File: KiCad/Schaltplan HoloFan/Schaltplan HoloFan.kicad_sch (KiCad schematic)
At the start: 23 parts, among them Q1 2N3904, Q2 2N3904, U1 NUCLEO-L432KC

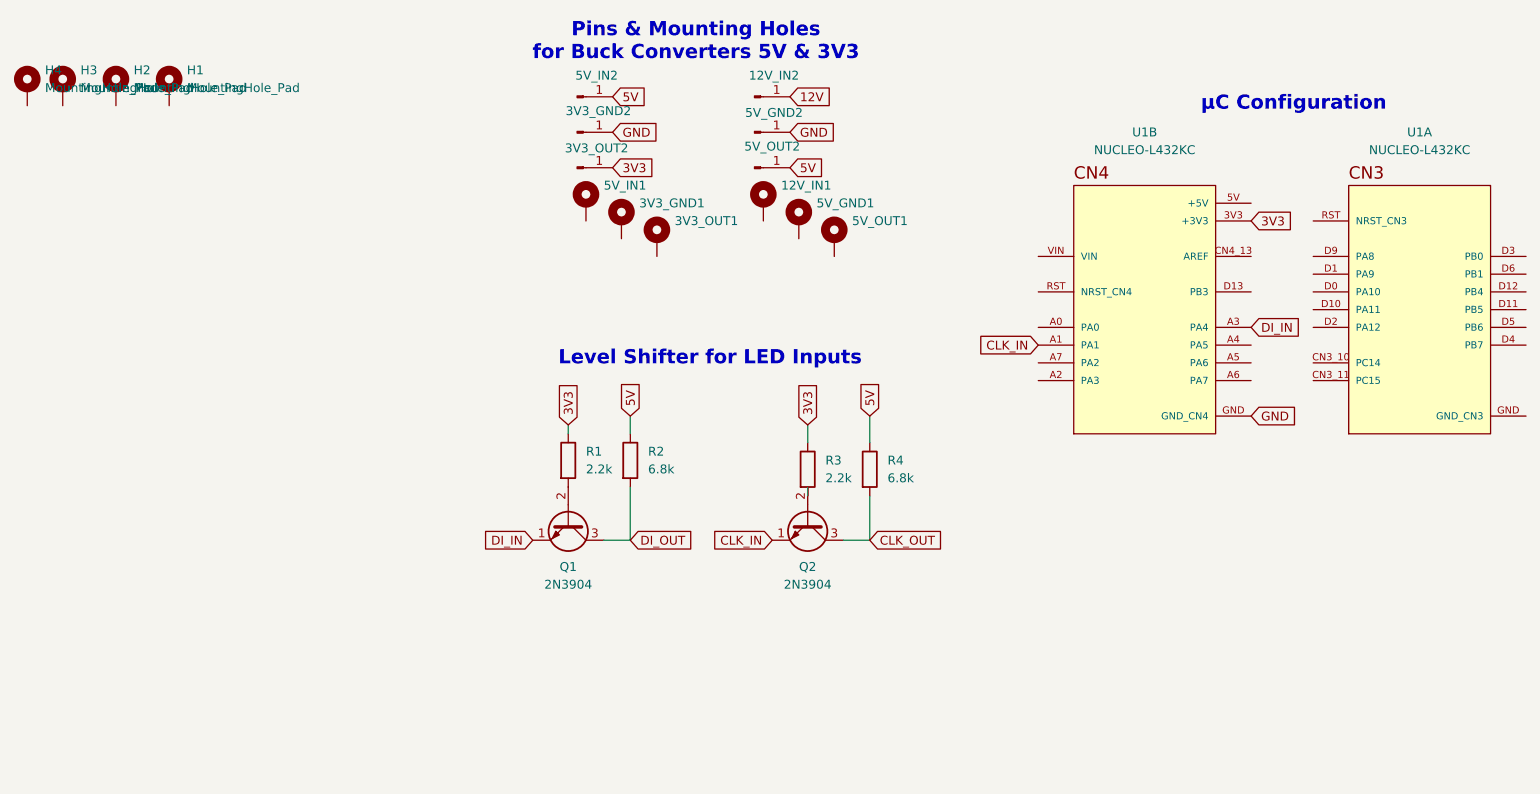
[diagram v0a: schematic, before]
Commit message: Python Programm Update + Timer Interrupt
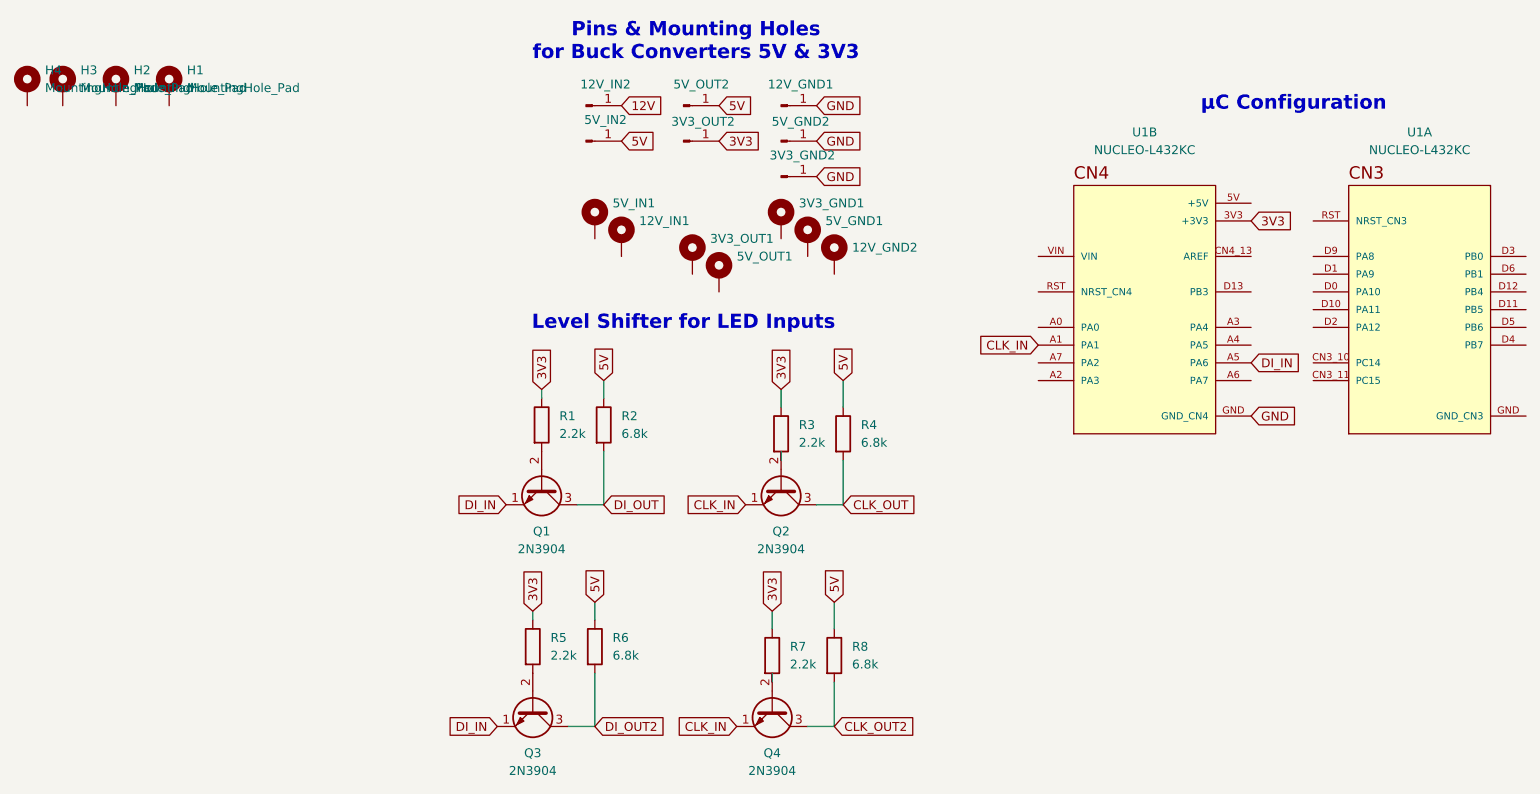
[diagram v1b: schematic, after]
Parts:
- added 12V_GND1: Conn_01x01_Pin, Connector_PinHeader_1.00mm:PinHeader_1x01_P1.00mm_Vertical, symbol Connector:Conn_01x01_Pin
- added 12V_GND2: MountingHole_Pad, MountingHole:MountingHole_2.2mm_M2, symbol Mechanical:MountingHole_Pad
- added Q3, Q4: 2N3904, Package_TO_SOT_THT:TO-92_Inline, symbol Transistor_BJT:2N3904
- added R5, R7: 2.2k, Resistor_THT:R_Axial_DIN0207_L6.3mm_D2.5mm_P7.62mm_Horizontal, symbol Device:R
- added R6, R8: 6.8k, Resistor_THT:R_Axial_DIN0207_L6.3mm_D2.5mm_P7.62mm_Horizontal, symbol Device:R
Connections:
- net 3V3: now also R5.1, R7.1
- net 5V: now also R6.1, R8.1
- net CLK_IN: now also Q4.1 (E)
- net DI_IN: now also U1.A5 (PA6), Q3.1 (E); no longer U1.A3 (PA4)
- net GND: now also 12V_GND1.1 (Pin_1)
- new net: Q4.2 (B), R7.2
- new net: Q3.2 (B), R5.2
- new net CLK_OUT2: Q4.3 (C), R8.2
- new net DI_OUT2: Q3.3 (C), R6.2
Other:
- moved on the sheet: 12V_IN1, 12V_IN2, 3V3_GND1, 3V3_GND2, 3V3_OUT1, 3V3_OUT2, 5V_GND1, 5V_GND2, 5V_IN1, 5V_IN2, 5V_OUT1, 5V_OUT2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

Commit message: Finishing of HoloFan Project
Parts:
- removed 12V_GND2, 12V_IN1, 3V3_GND1, 3V3_OUT1, 5V_GND1, 5V_IN1, 5V_OUT1: MountingHole_Pad, MountingHole:MountingHole_2.2mm_M2, symbol Mechanical:MountingHole_Pad
- removed H1, H2, H3, H4: MountingHole_Pad, symbol Mechanical:MountingHole_Pad
- removed Q3, Q4: 2N3904, Package_TO_SOT_THT:TO-92_Inline, symbol Transistor_BJT:2N3904
- removed R5, R7: 2.2k, Resistor_THT:R_Axial_DIN0207_L6.3mm_D2.5mm_P7.62mm_Horizontal, symbol Device:R
- removed R6, R8: 6.8k, Resistor_THT:R_Axial_DIN0207_L6.3mm_D2.5mm_P7.62mm_Horizontal, symbol Device:R
- added 5V_GND3: Conn_01x01_Pin, Connector_PinHeader_1.00mm:PinHeader_1x01_P1.00mm_Vertical, symbol Connector:Conn_01x01_Pin
- added LED_1, LED_2: Conn_01x04_Pin, APA102:APA102_Pads, symbol Connector:Conn_01x04_Pin
- Q1, Q2: footprint Package_TO_SOT_THT:TO-92_Inline -> Package_TO_SOT_SMD:TSOT-23
- R1, R2, R3, R4: footprint Resistor_THT:R_Axial_DIN0207_L6.3mm_D2.5mm_P7.62mm_Horizontal -> Resistor_SMD:R_0603_1608Metric
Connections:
- net 5V: now also LED_1.4 (Pin_4), LED_2.4 (Pin_4)
- net CLK_OUT: now also LED_1.2 (Pin_2), LED_2.2 (Pin_2)
- net DI_OUT: now also LED_1.3 (Pin_3), LED_2.3 (Pin_3)
- net GND: now also 5V_GND3.1 (Pin_1), LED_1.1 (Pin_1), LED_2.1 (Pin_1)
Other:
- moved on the sheet: Q1, Q2, R1, R2, R3, R4

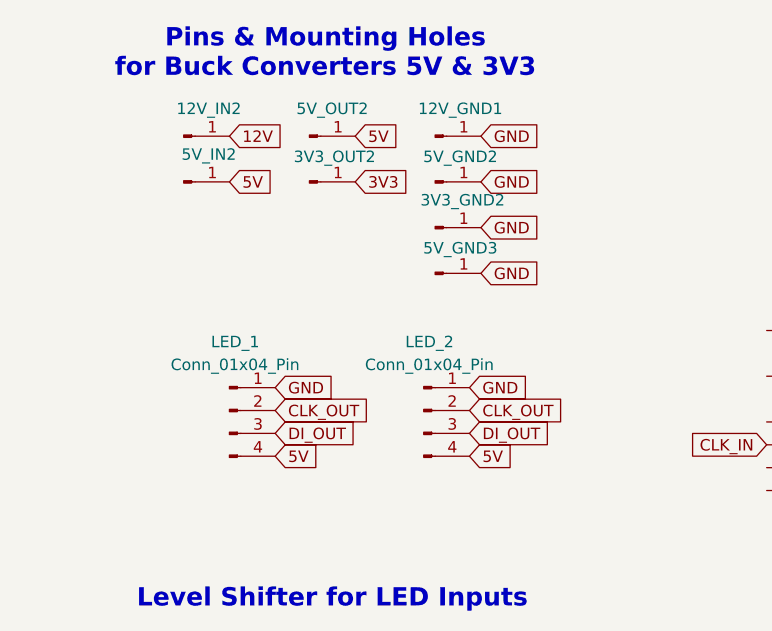
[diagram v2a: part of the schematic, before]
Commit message: PCB Layout Finishing
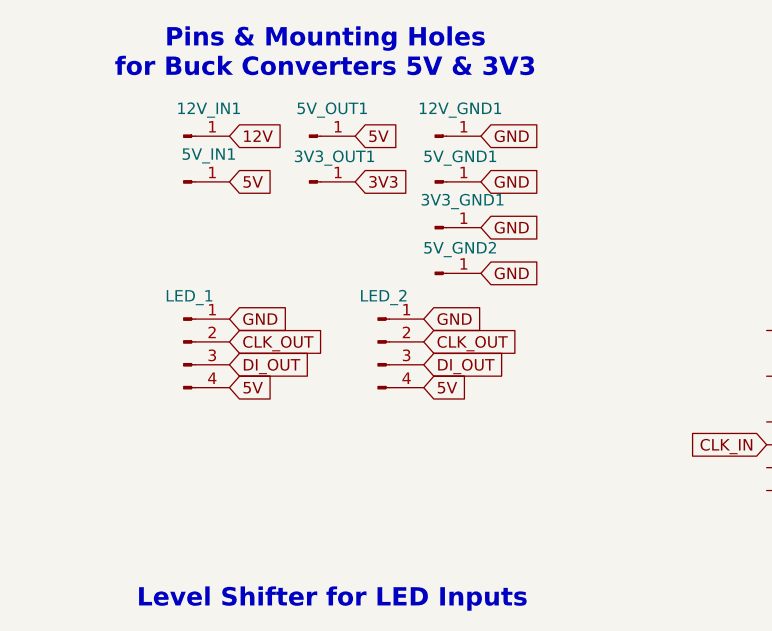
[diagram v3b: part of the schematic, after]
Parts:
- renumbered 12V_IN2 to 12V_IN1, 3V3_GND2 to 3V3_GND1, 3V3_OUT2 to 3V3_OUT1, 5V_GND2 to 5V_GND1, 5V_GND3 to 5V_GND2, 5V_IN2 to 5V_IN1, 5V_OUT2 to 5V_OUT1
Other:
- moved on the sheet: LED_1, LED_2
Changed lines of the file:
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@@
 	(global_label "DI_OUT"
 		(shape input)
-		(at 166.37 76.2 0)
+		(at 161.29 68.58 0)
 		(fields_autoplaced yes)
 		(effects
@@
 		)
 		(property "Intersheetrefs" "${INTERSHEET_REFS}"
-			(at 175.8262 76.2 0)
+			(at 170.7462 68.58 0)
 			(effects
 				(font
@@
 	(global_label "GND"
 		(shape input)
-		(at 166.37 71.12 0)
+		(at 161.29 63.5 0)
 		(fields_autoplaced yes)
 		(effects
@@
 		)
 		(property "Intersheetrefs" "${INTERSHEET_REFS}"
-			(at 173.2257 71.12 0)
+			(at 168.1457 63.5 0)
 			(effects
 				(font
@@
 	(global_label "GND"
 		(shape input)
-		(at 144.78 71.12 0)
+		(at 139.7 63.5 0)
 		(fields_autoplaced yes)
 		(effects
@@
 		)
 		(property "Intersheetrefs" "${INTERSHEET_REFS}"
-			(at 151.6357 71.12 0)
+			(at 146.5557 63.5 0)
 			(effects
 				(font
@@
 	(global_label "DI_OUT"
 		(shape input)
-		(at 144.78 76.2 0)
+		(at 139.7 68.58 0)
 		(fields_autoplaced yes)
 		(effects
@@
 		)
 		(property "Intersheetrefs" "${INTERSHEET_REFS}"
-			(at 154.2362 76.2 0)
+			(at 149.1562 68.58 0)
 			(effects
 				(font
@@
 	(global_label "5V"
 		(shape input)
-		(at 144.78 78.74 0)
+		(at 139.7 71.12 0)
 		(fields_autoplaced yes)
 		(effects
@@
 		)
 		(property "Intersheetrefs" "${INTERSHEET_REFS}"
-			(at 150.0633 78.74 0)
+			(at 144.9833 71.12 0)
 			(effects
 				(font
@@
 	(global_label "CLK_OUT"
 		(shape input)
-		(at 144.78 73.66 0)
+		(at 139.7 66.04 0)
 		(fields_autoplaced yes)
 		(effects
@@
 		)
 		(property "Intersheetrefs" "${INTERSHEET_REFS}"
-			(at 155.9295 73.66 0)
+			(at 150.8495 66.04 0)
 			(effects
 				(font
@@
 	(global_label "CLK_OUT"
 		(shape input)
-		(at 166.37 73.66 0)
+		(at 161.29 66.04 0)
 		(fields_autoplaced yes)
 		(effects
@@
 		)
 		(property "Intersheetrefs" "${INTERSHEET_REFS}"
-			(at 177.5195 73.66 0)
+			(at 172.4395 66.04 0)
 			(effects
 				(font
@@
 	(global_label "5V"
 		(shape input)
-		(at 166.37 78.74 0)
+		(at 161.29 71.12 0)
 		(fields_autoplaced yes)
 		(effects
@@
 		)
 		(property "Intersheetrefs" "${INTERSHEET_REFS}"
-			(at 171.6533 78.74 0)
+			(at 166.5733 71.12 0)
 			(effects
 				(font
@@
 		(on_board yes)
 		(dnp no)
-		(property "Reference" "3V3_GND2"
+		(property "Reference" "3V3_GND1"
 			(at 165.608 50.292 0)
 			(effects
@@
 			(project ""
 				(path "/3660609d-0404-43eb-9452-5e5c87515aaf"
-					(reference "3V3_GND2")
+					(reference "3V3_GND1")
 					(unit 1)
 				)
@@
 	(symbol
 		(lib_id "Connector:Conn_01x04_Pin")
-		(at 139.7 73.66 0)
+		(at 134.62 66.04 0)
 		(unit 1)
 		(exclude_from_sim no)
@@
 		(fields_autoplaced yes)
 		(property "Reference" "LED_1"
-			(at 140.335 66.04 0)
+			(at 135.255 60.96 0)
 			(effects
 				(font
@@
 		)
 		(property "Value" "Conn_01x04_Pin"
-			(at 140.335 68.58 0)
-			(effects
-				(font
-					(size 1.27 1.27)
-				)
+			(at 135.255 60.96 0)
+			(effects
+				(font
+					(size 1.27 1.27)
+				)
+				(hide yes)
 			)
 		)
 		(property "Footprint" "APA102:APA102_Pads"
-			(at 139.7 73.66 0)
+			(at 134.62 66.04 0)
 			(effects
 				(font
@@
 		)
 		(property "Datasheet" "~"
-			(at 139.7 73.66 0)
+			(at 134.62 66.04 0)
 			(effects
 				(font
@@
 		)
 		(property "Description" "Generic connector, single row, 01x04, script generated"
-			(at 139.7 73.66 0)
+			(at 134.62 66.04 0)
 			(effects
 				(font
@@
 		(on_board yes)
 		(dnp no)
-		(property "Reference" "5V_IN2"
+		(property "Reference" "5V_IN1"
 			(at 137.414 45.212 0)
 			(effects
@@
 			(project ""
 				(path "/3660609d-0404-43eb-9452-5e5c87515aaf"
-					(reference "5V_IN2")
+					(reference "5V_IN1")
 					(unit 1)
 				)
@@
 		(on_board yes)
 		(dnp no)
-		(property "Reference" "5V_OUT2"
+		(property "Reference" "5V_OUT1"
 			(at 151.13 40.132 0)
 			(effects
@@
 			(project ""
 				(path "/3660609d-0404-43eb-9452-5e5c87515aaf"
-					(reference "5V_OUT2")
+					(reference "5V_OUT1")
 					(unit 1)
 				)
@@
 		(on_board yes)
 		(dnp no)
-		(property "Reference" "5V_GND3"
+		(property "Reference" "5V_GND2"
 			(at 165.354 55.626 0)
 			(effects
@@
 			(project "Schaltplan HoloFan"
 				(path "/3660609d-0404-43eb-9452-5e5c87515aaf"
-					(reference "5V_GND3")
+					(reference "5V_GND2")
 					(unit 1)
 				)
@@
 		(on_board yes)
 		(dnp no)
-		(property "Reference" "5V_GND2"
+		(property "Reference" "5V_GND1"
 			(at 165.354 45.466 0)
 			(effects
@@
 			(project ""
 				(path "/3660609d-0404-43eb-9452-5e5c87515aaf"
-					(reference "5V_GND2")
+					(reference "5V_GND1")
 					(unit 1)
 				)
@@
 	(symbol
 		(lib_id "Connector:Conn_01x04_Pin")
-		(at 161.29 73.66 0)
+		(at 156.21 66.04 0)
 		(unit 1)
 		(exclude_from_sim no)
@@
 		(fields_autoplaced yes)
 		(property "Reference" "LED_2"
-			(at 161.925 66.04 0)
+			(at 156.845 60.96 0)
 			(effects
 				(font
@@
 		)
 		(property "Value" "Conn_01x04_Pin"
-			(at 161.925 68.58 0)
-			(effects
-				(font
-					(size 1.27 1.27)
-				)
+			(at 156.845 60.96 0)
+			(effects
+				(font
+					(size 1.27 1.27)
+				)
+				(hide yes)
 			)
 		)
 		(property "Footprint" "APA102:APA102_Pads"
-			(at 161.29 73.66 0)
+			(at 156.21 66.04 0)
 			(effects
 				(font
@@
 		)
 		(property "Datasheet" "~"
-			(at 161.29 73.66 0)
+			(at 156.21 66.04 0)
 			(effects
 				(font
@@
 		)
 		(property "Description" "Generic connector, single row, 01x04, script generated"
-			(at 161.29 73.66 0)
+			(at 156.21 66.04 0)
 			(effects
 				(font
@@
 		(on_board yes)
 		(dnp no)
-		(property "Reference" "12V_IN2"
+		(property "Reference" "12V_IN1"
 			(at 137.414 40.132 0)
 			(effects
@@
 			(project ""
 				(path "/3660609d-0404-43eb-9452-5e5c87515aaf"
-					(reference "12V_IN2")
+					(reference "12V_IN1")
 					(unit 1)
 				)
@@
 		(on_board yes)
 		(dnp no)
-		(property "Reference" "3V3_OUT2"
+		(property "Reference" "3V3_OUT1"
 			(at 151.384 45.466 0)
 			(effects
@@
 			(project ""
 				(path "/3660609d-0404-43eb-9452-5e5c87515aaf"
-					(reference "3V3_OUT2")
+					(reference "3V3_OUT1")
 					(unit 1)
 				)
